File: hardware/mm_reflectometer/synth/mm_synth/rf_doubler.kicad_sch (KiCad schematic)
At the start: 8 parts

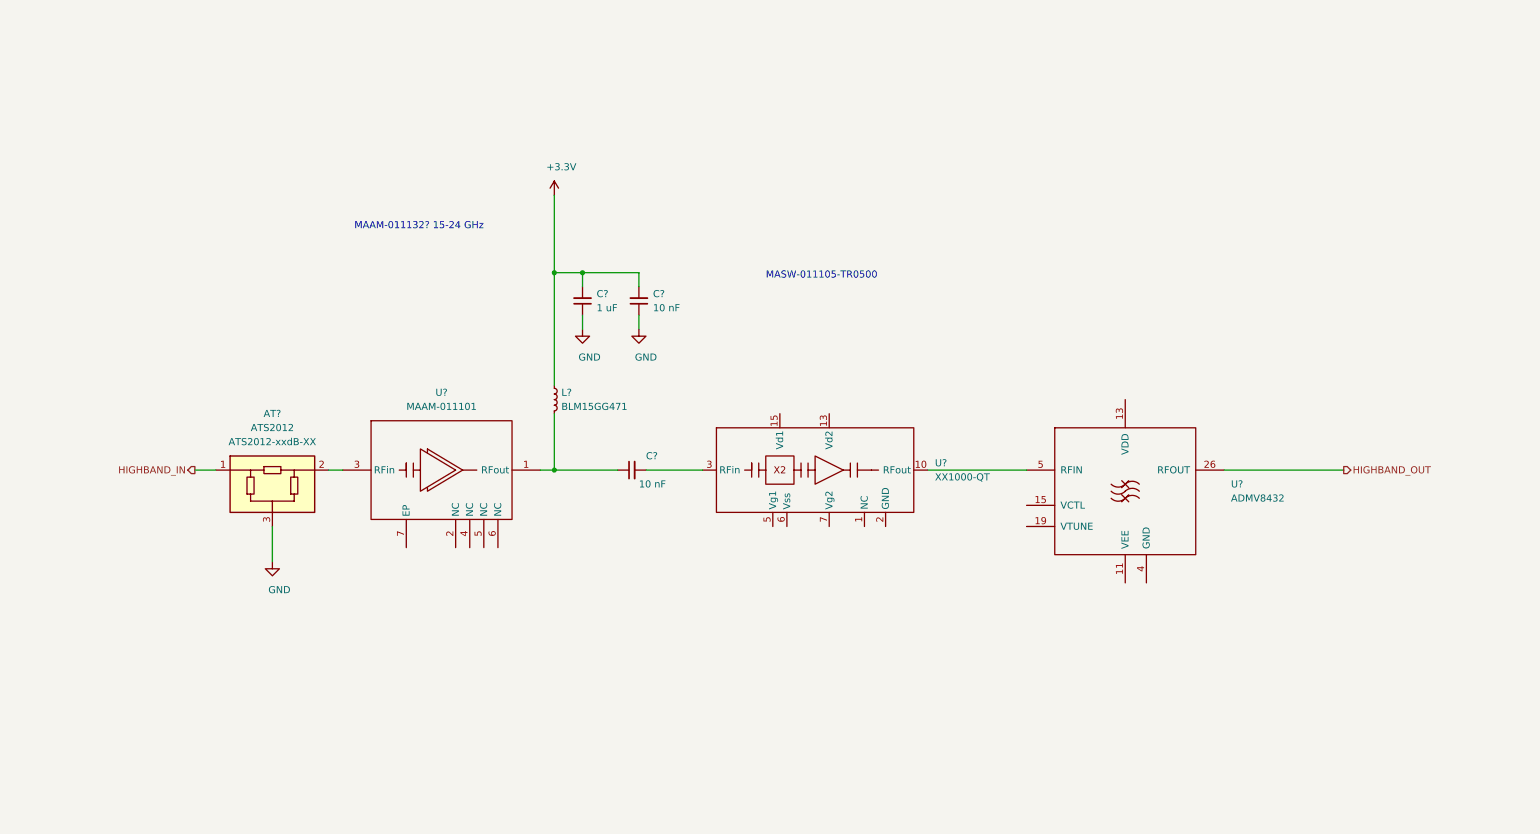
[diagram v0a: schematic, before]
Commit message: adding bias circuitry to mm synth
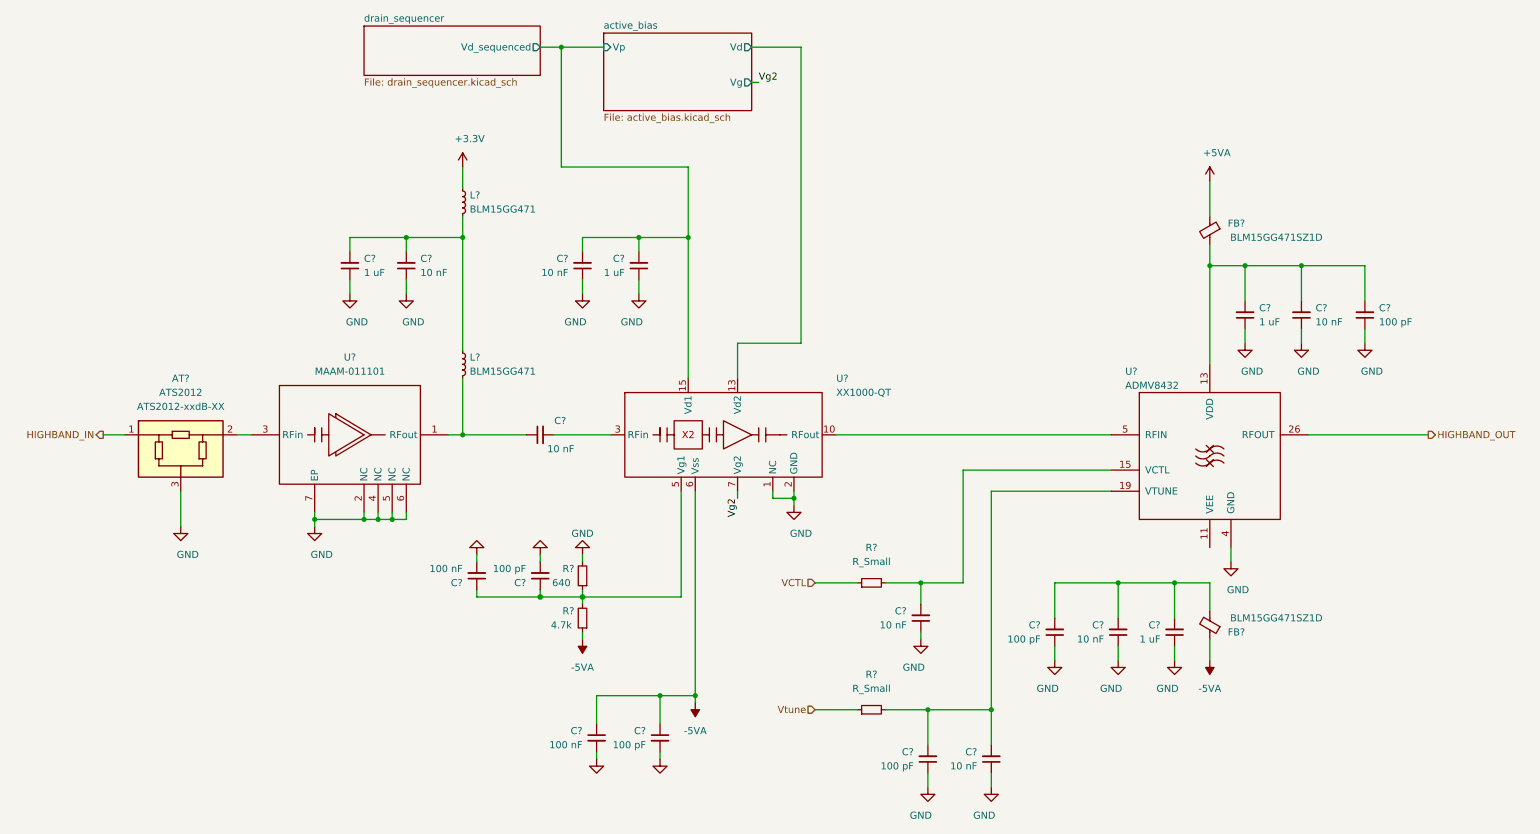
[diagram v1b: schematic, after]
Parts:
- added C? (x2): 100 nF, Capacitor_SMD:C_0402_1005Metric, symbol Device:C_Small
- added C? (x5): 10 nF, symbol Device:C_Small
- added C? (x3): 1 uF, symbol Device:C_Small
- added C? (x3): 100 pF, symbol Device:C_Small
- added C? (x2): 100 pF, Capacitor_SMD:C_0402_1005Metric, symbol Device:C_Small
- added FB? (x2): BLM15GG471SZ1D, symbol Device:FerriteBead_Small
- added L?: BLM15GG471, symbol Device:L_Small
- added R?: 640, Resistor_SMD:R_0402_1005Metric, symbol Device:R_Small
- added R? (x2): R_Small, symbol Device:R_Small
- added R?: 4.7k, Resistor_SMD:R_0402_1005Metric, symbol Device:R_Small
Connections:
- net +3V3: now also L?.1; no longer C?.2, C?.2, L?.1
- net GND: now also U?.1 (NC), U?.11 (GND), U?.12 (NC), U?.14 (NC), U?.16 (NC), U?.17 (GND), U?.2 (GND), U?.2 (NC), U?.4 (GND), U?.4 (NC), U?.5 (NC), U?.6 (NC), U?.7 (EP), U?.8 (NC), U?.9 (GND), C?.1, C?.1, C?.1, C?.1, C?.1, C?.1, C?.1, C?.1, C?.1, C?.1, C?.1, C?.2, C?.2, C?.2, C?.2, R?.2
- net active_bias/Vd: now reaches U?.13 (Vd2)
- net active_bias/Vp: now reaches U?.15 (Vd1)
- net active_bias/Vp: now also C?.2, C?.2
- net at U?.5 (Vg1): now also C?.1, C?.1, R?.1, R?.2
- net -5VA: now reaches U?.6 (Vss)
- net -5VA: now also C?.1, C?.1, FB?.1, R?.1
- net Vg2: now reaches U?.7 (Vg2)
- net at U?.13 (VDD): now also C?.2, C?.2, C?.2, FB?.2
- net at U?.15 (VCTL): now also C?.2, R?.2
- net at U?.19 (VTUNE): now also C?.2, C?.2, R?.2
- new net: C?.2, C?.2, L?.1, L?.2
- new net: C?.2, C?.2, C?.2, FB?.2
- new net +5VA: FB?.1
- new net VCTL: R?.1
- new net Vtune: R?.1
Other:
- added sheet active_bias (active_bias.kicad_sch)
- added sheet drain_sequencer (drain_sequencer.kicad_sch)
- note removed: "MAAM-011132? 15-24 GHz"
- note removed: "MASW-011105-TR0500"
- moved on the sheet: AT?, C?, L?, U?

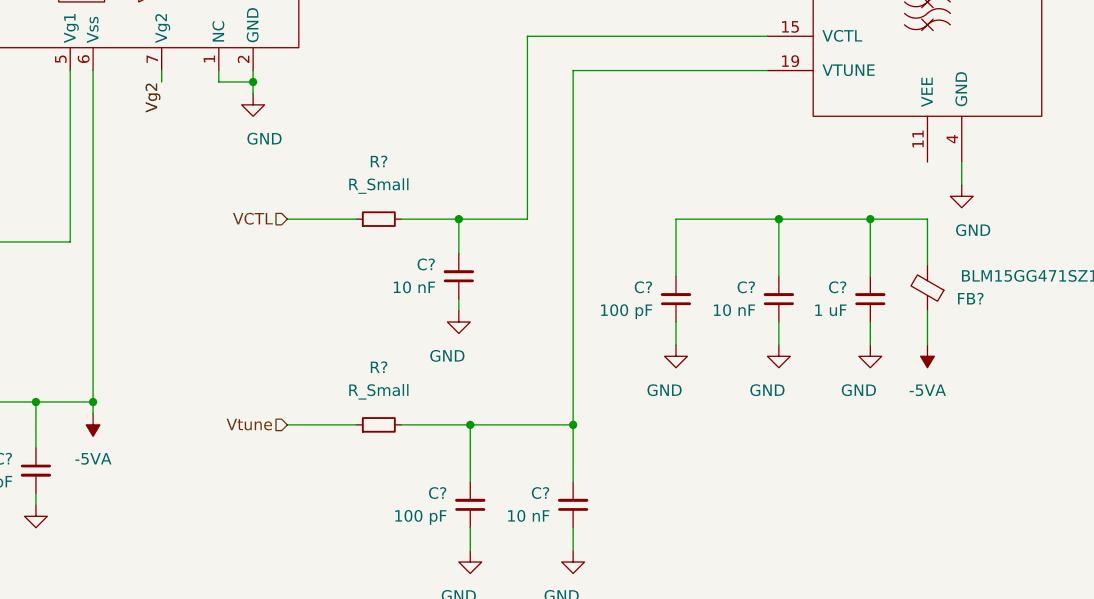
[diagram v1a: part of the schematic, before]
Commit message: added dac to mm_synth for vtune/adjstable bias, added ADC for telemetry
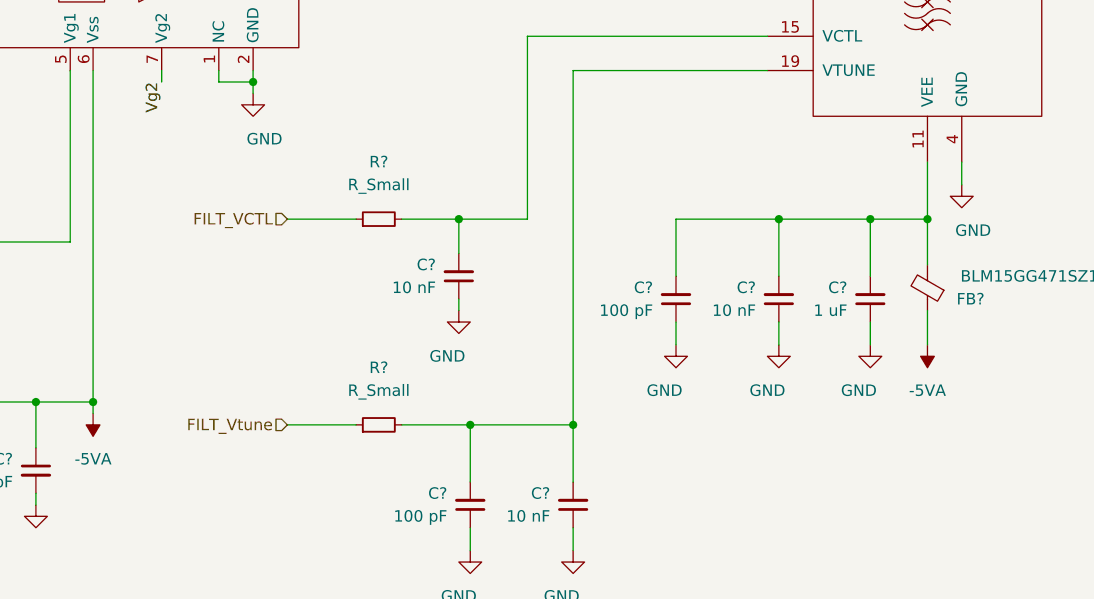
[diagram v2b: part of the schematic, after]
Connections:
- net at C?.2, C?.2, C?.2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: now also U?.11 (VEE)
- net VCTL renamed FILT_VCTL
- net Vtune renamed FILT_Vtune
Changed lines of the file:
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@@
   (junction (at 219.71 118.11) (diameter 0.9144) (color 0 0 0 0))
   (junction (at 226.06 60.96) (diameter 0.9144) (color 0 0 0 0))
+  (junction (at 226.06 118.11) (diameter 0.9144) (color 0 0 0 0))
   (junction (at 232.41 60.96) (diameter 0.9144) (color 0 0 0 0))
   (junction (at 242.57 60.96) (diameter 0.9144) (color 0 0 0 0))
@@
     (stroke (width 0) (type solid) (color 0 0 0 0))
   )
+  (wire (pts (xy 226.06 111.76) (xy 226.06 118.11))
+    (stroke (width 0) (type solid) (color 0 0 0 0))
+  )
   (wire (pts (xy 226.06 118.11) (xy 226.06 123.19))
     (stroke (width 0) (type solid) (color 0 0 0 0))
@@
     (effects (font (size 1.27 1.27)) (justify right))
   )
-  (hierarchical_label "VCTL" (shape input) (at 154.94 118.11 180)
+  (hierarchical_label "FILT_VCTL" (shape input) (at 154.94 118.11 180)
     (effects (font (size 1.27 1.27)) (justify right))
   )
-  (hierarchical_label "Vtune" (shape input) (at 154.94 140.97 180)
+  (hierarchical_label "FILT_Vtune" (shape input) (at 154.94 140.97 180)
     (effects (font (size 1.27 1.27)) (justify right))
   )

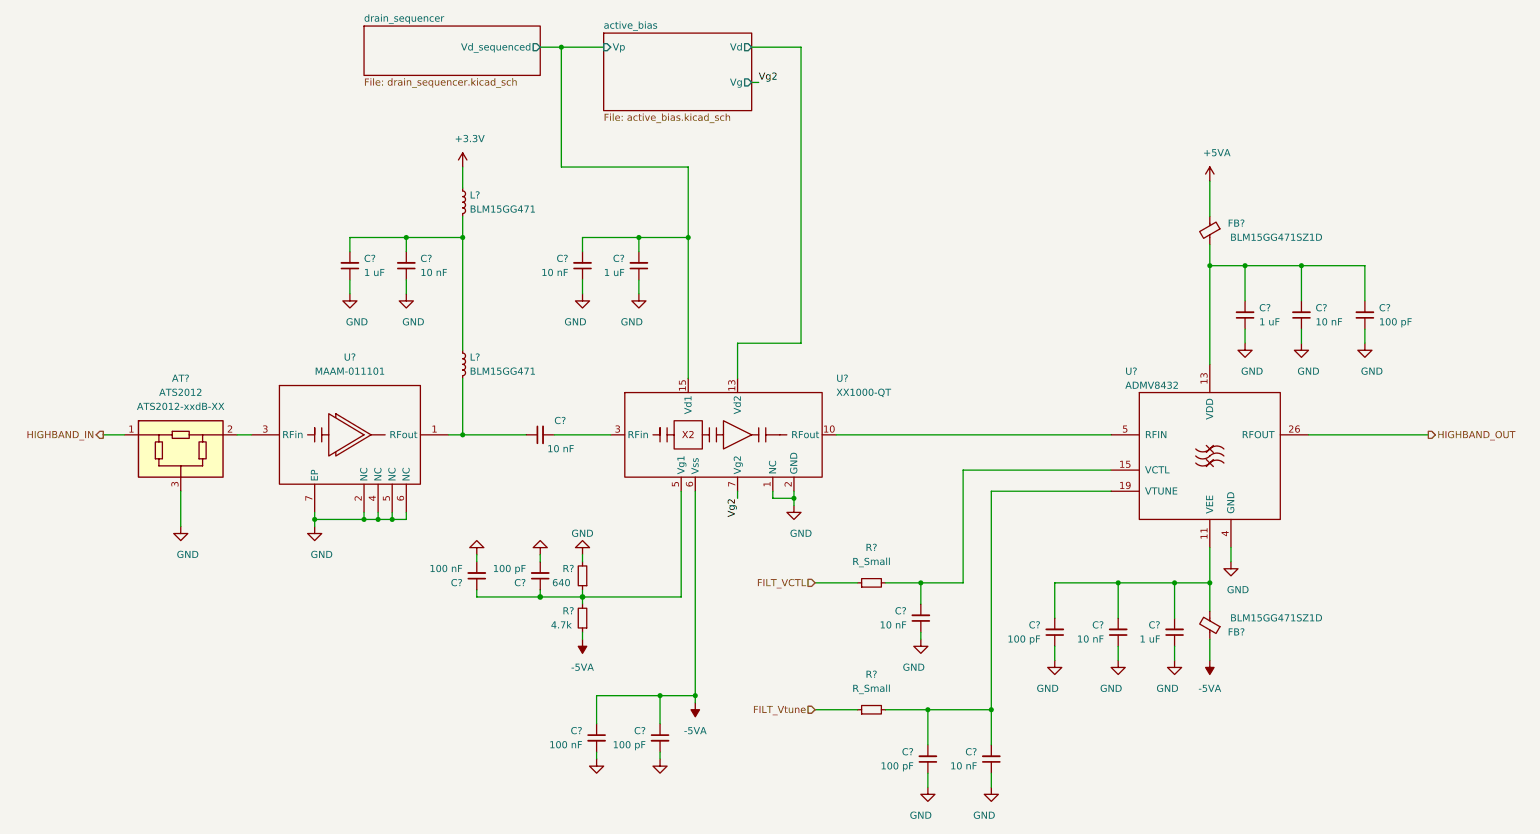
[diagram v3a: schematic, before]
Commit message: adding digital connections to synth schematic
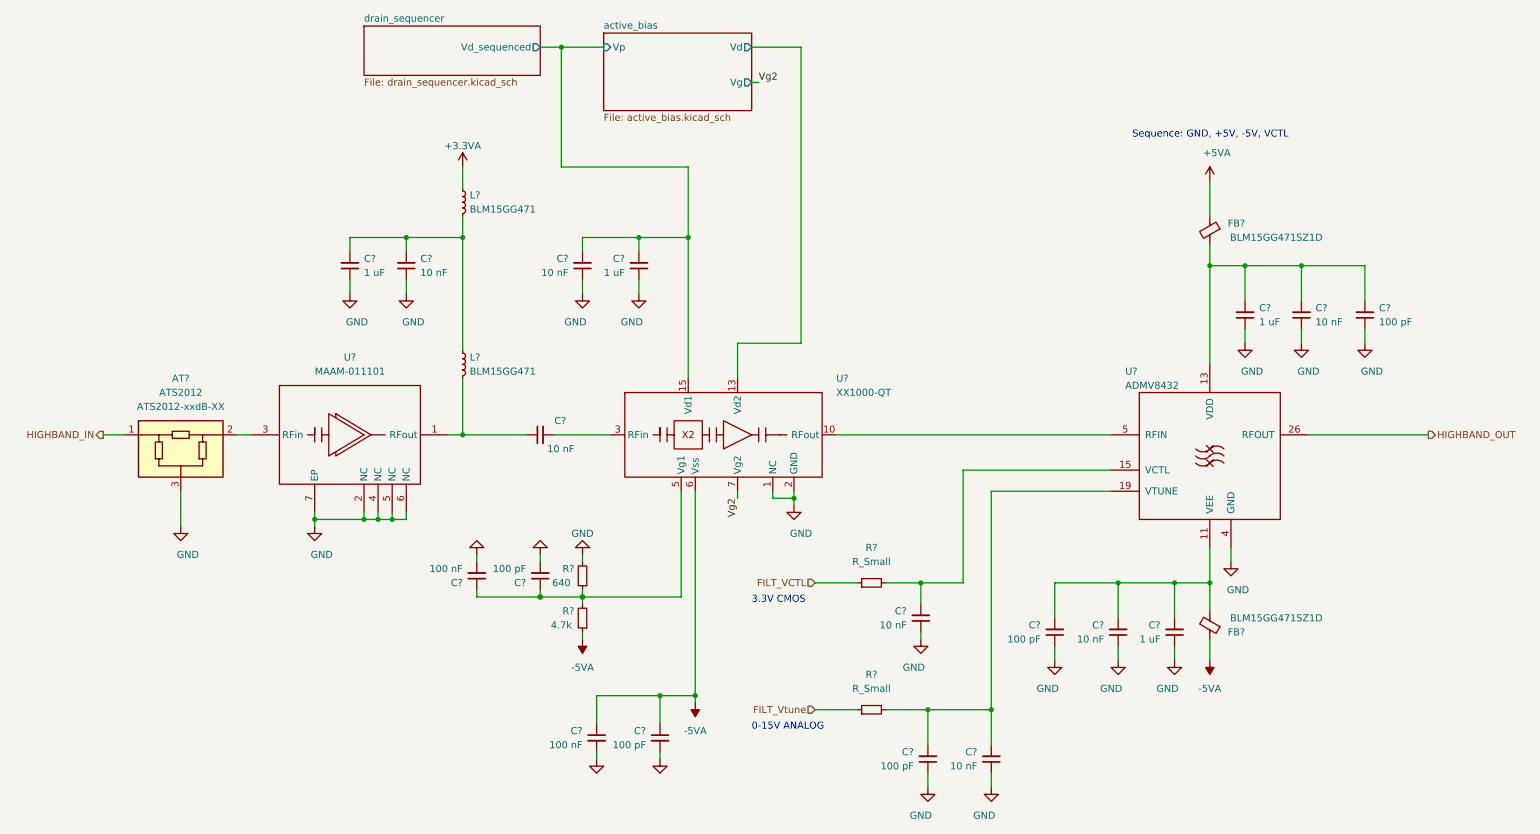
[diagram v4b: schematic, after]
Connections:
- net +3V3 renamed +3.3VA
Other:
- note added: "0-15V ANALOG"
- note added: "3.3V CMOS"
- note added: "Sequence: GND, +5V, -5V, VCTL"
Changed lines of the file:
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@@
     (stroke (width 0) (type solid) (color 0 0 0 0))
+  )
+  (text "3.3V CMOS" (at 143.51 121.92 0)
+    (effects (font (size 1.27 1.27)) (justify left bottom))
+  )
+  (text "0-15V ANALOG" (at 143.51 144.78 0)
+    (effects (font (size 1.27 1.27)) (justify left bottom))
+  )
+  (text "Sequence: GND, +5V, -5V, VCTL" (at 212.09 38.1 0)
+    (effects (font (size 1.27 1.27)) (justify left bottom))
   )
   (label "Vg2" (at 140.97 102.87 270)
@@
     (effects (font (size 1.27 1.27)) (justify left))
   )
-  (symbol (lib_id "power:+3.3V") (at 91.44 43.18 0) (unit 1)
-    (in_bom yes) (on_board yes)
-    (property "Reference" "#PWR0222" (id 0) (at 91.44 46.99 0)
+  (symbol (lib_id "power:+3.3VA") (at 91.44 43.18 0) (unit 1)
+    (in_bom yes) (on_board yes) (fields_autoplaced)
+    (property "Reference" "#PWR?" (id 0) (at 91.44 46.99 0)
       (effects (font (size 1.27 1.27)) hide)
     )
-    (property "Value" "+3.3V" (id 1) (at 92.71 38.1 0))
+    (property "Value" "+3.3VA" (id 1) (at 91.44 39.37 0))
     (property "Footprint" "" (id 2) (at 91.44 43.18 0)
       (effects (font (size 1.27 1.27)) hide)

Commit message: work on mm synth schematic - control signals and footprint assignments
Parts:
- removed L? (x2): BLM15GG471, symbol Device:L_Small
- added FB501, FB502: BLM15GG471, symbol Device:FerriteBead_Small
- C501, C502, C504, C506, C508, C510, C511, C512, C513, C514, C515, C516, C517, C518: renamed from C?; footprint (none) -> Capacitor_SMD:C_0402_1005Metric
- R503, R504: renamed from R?; footprint (none) -> Resistor_SMD:R_0402_1005Metric
- gave numbers to parts that had none: 12
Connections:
- net +3.3VA: now also FB501.1
- net at C501.2, C502.2: now also FB501.2, FB502.1
- net at C504.1, U501.1 (RFout): now also FB502.2

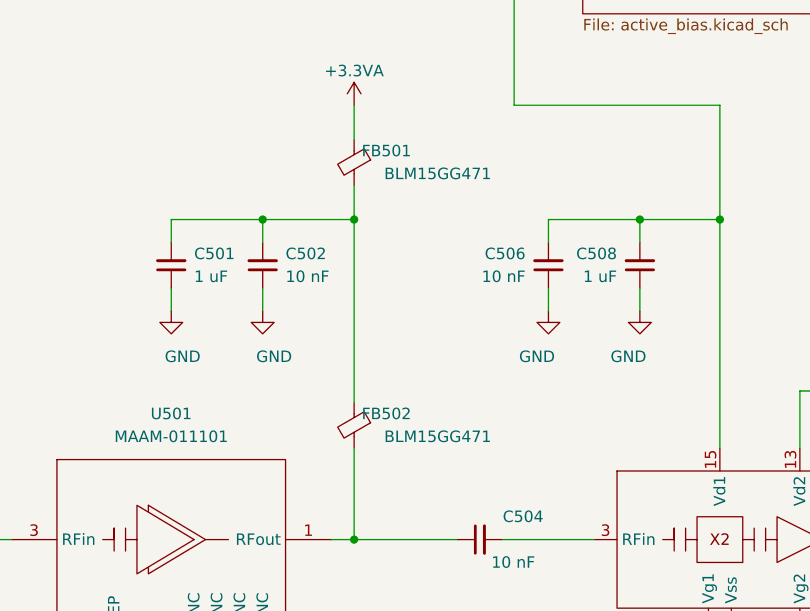
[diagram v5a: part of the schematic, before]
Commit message: added aux high speed io connector, fixed hierarchical buses
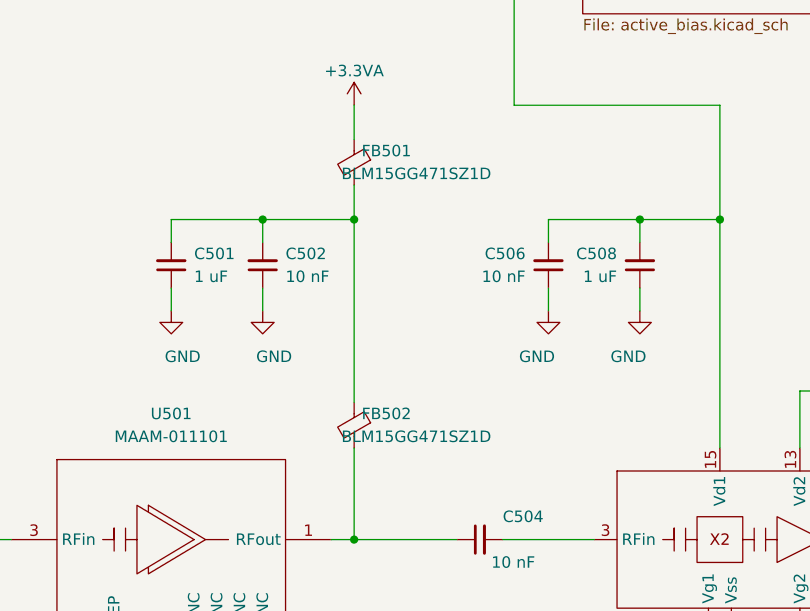
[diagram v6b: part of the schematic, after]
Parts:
- FB501, FB502: value BLM15GG471 -> BLM15GG471SZ1D; footprint (none) -> Inductor_SMD:L_0402_1005Metric
- FB503, FB504: footprint (none) -> Inductor_SMD:L_0402_1005Metric
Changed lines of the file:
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@@
       (effects (font (size 1.27 1.27)) (justify left))
     )
-    (property "Value" "BLM15GG471" (id 1) (at 106.68 50.8 0)
+    (property "Value" "BLM15GG471SZ1D" (id 1) (at 106.68 50.8 0)
       (effects (font (size 1.27 1.27)) (justify left))
     )
-    (property "Footprint" "" (id 2) (at 93.218 49.53 90)
+    (property "Footprint" "Inductor_SMD:L_0402_1005Metric" (id 2) (at 93.218 49.53 90)
       (effects (font (size 1.27 1.27)) hide)
     )
@@
       (effects (font (size 1.27 1.27)) (justify left))
     )
-    (property "Value" "BLM15GG471" (id 1) (at 106.68 80.01 0)
+    (property "Value" "BLM15GG471SZ1D" (id 1) (at 106.68 80.01 0)
       (effects (font (size 1.27 1.27)) (justify left))
     )
-    (property "Footprint" "" (id 2) (at 93.218 78.74 90)
+    (property "Footprint" "Inductor_SMD:L_0402_1005Metric" (id 2) (at 93.218 78.74 90)
       (effects (font (size 1.27 1.27)) hide)
     )
@@
       (effects (font (size 1.27 1.27)) (justify left))
     )
-    (property "Footprint" "" (id 2) (at 227.838 54.61 90)
+    (property "Footprint" "Inductor_SMD:L_0402_1005Metric" (id 2) (at 227.838 54.61 90)
       (effects (font (size 1.27 1.27)) hide)
     )
@@
       (effects (font (size 1.27 1.27)) (justify left))
     )
-    (property "Footprint" "" (id 2) (at 227.838 125.73 90)
+    (property "Footprint" "Inductor_SMD:L_0402_1005Metric" (id 2) (at 227.838 125.73 90)
       (effects (font (size 1.27 1.27)) hide)
     )
